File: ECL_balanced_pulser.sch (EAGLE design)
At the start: 41 parts, among them Q1 BC636, T1 2N2369, U1 MC100EPT22DG, U2 MAX961ESA+, X1 BU-SMA-H, X2 BU-SMA-H, X3 BU-SMA-H

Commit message: added a small copyright note
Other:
- note added: "Copyright 2015 by Mathias Helsen, MIT license"
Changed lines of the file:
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@@
 <sheet>
 <plain>
+<text x="40.64" y="114.3" size="1.778" layer="91">Copyright 2015 by Mathias Helsen, MIT license</text>
 </plain>
 <instances>

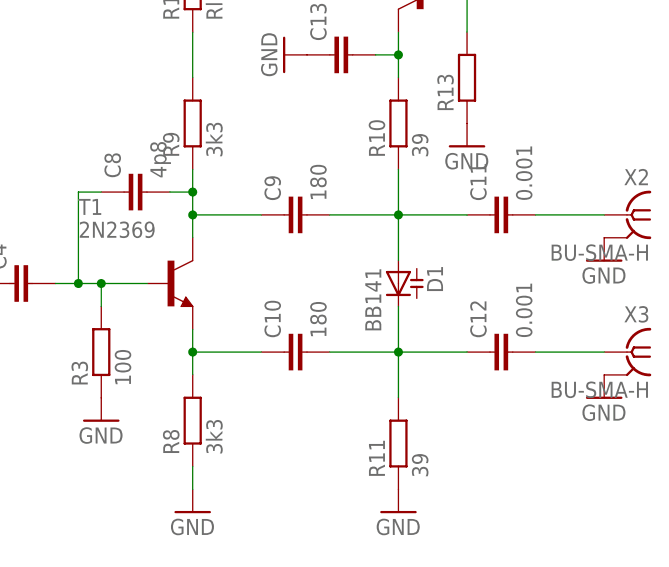
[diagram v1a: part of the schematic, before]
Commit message: custom footprint for 2D524A SRD
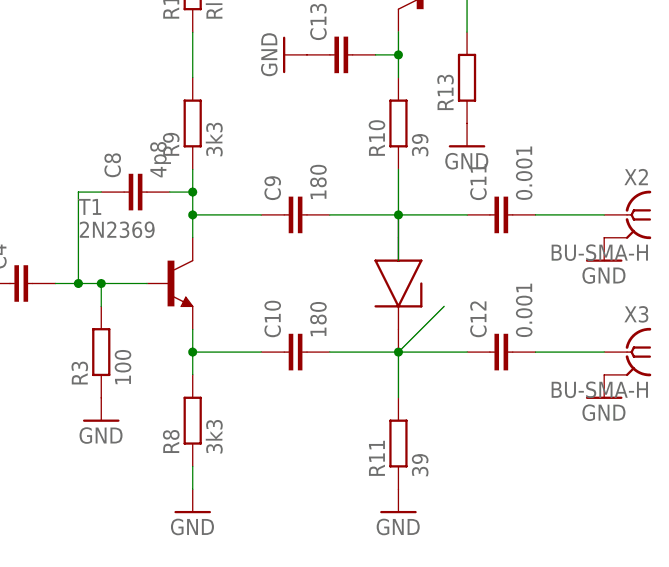
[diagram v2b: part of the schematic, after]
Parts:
- removed D1: BB141, diode:BB141
- added U$2: 2D524A, srd:2D524A
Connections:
- net N$14: now also U$2.ANODE; no longer D1.A
- net N$16: now also U$2.CATHODE; no longer D1.C
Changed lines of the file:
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@@
 <part name="C9" library="resistor" deviceset="C-EU" device="C0805" value="180"/>
 <part name="C10" library="resistor" deviceset="C-EU" device="C0805" value="180"/>
-<part name="D1" library="diode" deviceset="BB141" device=""/>
 <part name="R10" library="resistor" deviceset="R-EU_" device="R0805" value="39"/>
 <part name="R11" library="resistor" deviceset="R-EU_" device="R0805" value="39"/>
@@
 <part name="R15" library="resistor" deviceset="R-EU_" device="R0805"/>
 <part name="Q1" library="transistor-pnp" deviceset="BC636*" device=""/>
+<part name="U$2" library="srd" deviceset="2D524A" device=""/>
 </parts>
 <sheets>
@@
 <instance part="C9" gate="G$1" x="162.56" y="96.52" rot="R90"/>
 <instance part="C10" gate="G$1" x="162.56" y="81.28" rot="R90"/>
-<instance part="D1" gate="G$1" x="175.26" y="88.9" rot="R270"/>
 <instance part="R10" gate="G$1" x="175.26" y="106.68" rot="R90"/>
 <instance part="R11" gate="G$1" x="175.26" y="71.12" rot="R90"/>
@@
 <instance part="R15" gate="G$1" x="175.26" y="149.86" rot="R90"/>
 <instance part="Q1" gate="G$1" x="177.8" y="121.92" rot="MR0"/>
+<instance part="U$2" gate="G$1" x="175.26" y="83.82" rot="R270"/>
 </instances>
 <busses>
@@
 <pinref part="C11" gate="G$1" pin="1"/>
 <wire x1="167.64" y1="96.52" x2="175.26" y2="96.52" width="0.1524" layer="91"/>
-<pinref part="D1" gate="G$1" pin="A"/>
 <wire x1="175.26" y1="96.52" x2="182.88" y2="96.52" width="0.1524" layer="91"/>
 <wire x1="175.26" y1="91.44" x2="175.26" y2="96.52" width="0.1524" layer="91"/>
@@
 <pinref part="R10" gate="G$1" pin="1"/>
 <wire x1="175.26" y1="101.6" x2="175.26" y2="96.52" width="0.1524" layer="91"/>
+<pinref part="U$2" gate="G$1" pin="ANODE"/>
 </segment>
 </net>
@@
 <segment>
 <pinref part="R11" gate="G$1" pin="2"/>
-<pinref part="D1" gate="G$1" pin="C"/>
 <wire x1="175.26" y1="76.2" x2="175.26" y2="81.28" width="0.1524" layer="91"/>
 <pinref part="C10" gate="G$1" pin="2"/>
-<wire x1="175.26" y1="81.28" x2="175.26" y2="86.36" width="0.1524" layer="91"/>
+<wire x1="175.26" y1="81.28" x2="180.34" y2="86.36" width="0.1524" layer="91"/>
 <wire x1="167.64" y1="81.28" x2="175.26" y2="81.28" width="0.1524" layer="91"/>
 <junction x="175.26" y="81.28"/>
 <pinref part="C12" gate="G$1" pin="1"/>
 <wire x1="175.26" y1="81.28" x2="182.88" y2="81.28" width="0.1524" layer="91"/>
-</segment>
-</net>
+<pinref part="U$2" gate="G$1" pin="CATHODE"/>
+</segment>
+</net>
